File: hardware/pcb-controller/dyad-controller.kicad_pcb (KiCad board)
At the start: 2 copper layers, 35 x 50 mm, 45 parts, among them J1 USB_C_Receptacle_USB2.0, J10 USB-C split link, J2 SWD, J6 HC-FPC-0.5-20P-FH20, J7 HC-FPC-0.5-20P-FH20, J8 HC-FPC-0.5-14P-FH20, J9 USB-C split link, SW1 BOOTSEL, SW2 RESET, U1 W25Q128JVS, U2 USBLC6-2SC6, U3 RP2040, U4 XC6206PxxxMR-Regulator_Linear, Y1 12MHz

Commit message: Swap the controller crystal to the RP2040 minimal design's ABM8-272-T3
Found by the CONTROLLER.md §6 checklist, item 3. The reference design's
crystal was LCSC C9002 (YXC X322512MSB4SI): CL 20 pF and ESR 80 ohm,
loaded with 22 pF caps. That gives ~11 + 3 pF stray = ~14 pF against the
20 pF it needs, so it would run fast; and its ESR is above the 50 ohm that
Hardware design with RP2040 §2.3 assumes when sizing the 1 kOhm XOUT
resistor, so start-up margin was unknown. The guide says any other crystal
circuit "will require extensive testing".

Now the guide's circuit unchanged: Abracon ABM8-272-T3 (LCSC C20625731,
CL 10 pF, ESR <= 50 ohm) with two 15 pF C0G caps (C2/C3, LCSC C1548, JLCPCB
Basic) and R7 at 1 kOhm -- 7.5 pF + ~3 pF stray = 10.5 pF.

Same 3.2 x 2.5 mm 4-pad package with crystal on pins 1/3 and ground on
2/4, so the footprint and routing are untouched; only Y1's LCSC and
description and C2/C3's value and LCSC change, mirrored onto the board
footprints. CONTROLLER.md's BOM and §4 "transfers unchanged" list updated.

ERC unchanged at 152. DRC: 0 errors, 0 unconnected. Parity: 14.

Co-Authored-By: Claude Opus 5.5 <noreply@anthropic.com>
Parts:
- C2, C3: value 22pF -> 15pF
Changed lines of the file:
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@@
 			)
 		)
-		(property "Value" "22pF"
+		(property "Value" "15pF"
 			(at 0 -1.16 90)
 			(layer "B.Fab")
@@
 			)
 		)
-		(property "LCSC" "C1555"
+		(property "LCSC" "C1548"
 			(at 128.606875 285.547125 0)
 			(layer "B.Fab")
@@
 			)
 		)
-		(property "Value" "22pF"
+		(property "Value" "15pF"
 			(at 0 -1.16 270)
 			(layer "B.Fab")
@@
 			)
 		)
-		(property "LCSC" "C1555"
+		(property "LCSC" "C1548"
 			(at 278.590375 -122.158125 0)
 			(layer "B.Fab")
@@
 			)
 		)
-		(property "Description" ""
+		(property "Description" "Abracon ABM8-272-T3, 12 MHz, CL 10 pF, ESR 50 ohm max -- the crystal of the RP2040 minimal design"
 			(at 0 0 0)
 			(layer "F.Fab")
@@
 			)
 		)
-		(property "LCSC" "C9002"
+		(property "LCSC" "C20625731"
 			(at 0 0 0)
 			(layer "B.Fab")

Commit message: Remove the SWD header, move the RP2040 block forward, reroute with USB on B.Cu
The §6 checklist failed item 5: D+ 18 mm, D- 26 mm, six vias. Several
attempts to reroute USB in place left gaps, because the corridor from J1 to
U3 had no room for the nets that have to hop beside the pair.

- J2 (1x05 SWD socket, 13.8 x 3.6 mm through-hole) removed from schematic
  and board, with its wiring, labels and power symbols; U3's SWCLK/SWDIO
  get no-connect flags. Flashing is over USB with BOOTSEL. ERC 152 -> 145,
  no new findings.
- U3 with all its decoupling, the crystal network, R5/R6 and the flash
  with C1/R1 moved 4 mm forward as one group into the freed space; U2 a
  further 1 mm so a via fits beside its +5V pin, which sits between its
  two USB pins.
- USB routed by hand-written router on B.Cu: D+ 15.9 mm, D- 16.1 mm, no
  vias. The rest by Freerouting around it; then +5V to U2 and one GPIO1
  hop at J7 routed by the same router, 11 vias moved for hole spacing, a
  VBUS track at J1 necked to 0.3 mm, GND fills with 76 stitching vias, C13's
  GND pad solid. JLC marker moved clear of C15.

Against 2dc9af0: total track 2,167 -> 1,915 mm; F.Cu fill 48% in 5 pieces
-> 46% in 4, largest 656 -> 774 mm^2; B.Cu 47% in 16 -> 49% in 9, largest
738 -> 803 mm^2. Ground under USB 4% -> 9%, crystal 42% -> 27%, QSPI 26% ->
1% -- the matrix bundle still crosses beneath them on F.Cu.

CONTROLLER.md: J2's removal recorded, and the §6 checklist results added
(items 1-3, 8 pass; 4, 5 partial; 6, 7 open), with a correction to the
claim that no matrix crosses this board.

DRC: 0 errors, 0 unconnected. Parity: 14 field-copy differences.

Co-Authored-By: Claude Opus 5.5 <noreply@anthropic.com>
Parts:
- removed J2: SWD, Connector_PinSocket_2.54mm:PinSocket_1x05_P2.54mm_Vertical
- moved U1 4.00 mm to (207.3, 65.4)
- moved C1 4.00 mm to (204.2, 61.6)
- moved C10 4.00 mm to (200.5, 81.6)
- moved C11 4.00 mm to (194.1, 77.0)
- moved C12 4.00 mm to (207.6, 76.2)
- moved C14 4.00 mm to (194.9, 69.1)
- moved C15 4.00 mm to (206.6, 70.4)
- moved C2 4.00 mm to (207.1, 85.5)
- moved C3 4.00 mm to (200.4, 85.2)
- moved C5 4.00 mm to (199.9, 66.0)
- moved C6 4.00 mm to (198.9, 81.6)
- moved C9 4.00 mm to (194.9, 70.6)
- moved R1 4.00 mm to (210.9, 61.4)
- moved R5 4.00 mm to (201.1, 63.0)
- moved R6 4.00 mm to (199.3, 63.0)
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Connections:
- U3 pad 24: SWCLK -> unconnected-(U3-SWCLK-Pad24)
- U3 pad 25: SWD -> unconnected-(U3-SWDIO-Pad25)
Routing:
- net /GPIO12: track 86.8 -> 39.8 mm, vias 5 -> 3
- net SWCLK: track 26.6 -> 0.00 mm, vias 2 -> 0
- net /GPIO8: track 81.2 -> 55.8 mm
- net SWD: track 25.1 -> 0.00 mm
- net /GPIO15: track 74.6 -> 51.1 mm, vias 5 -> 2
- net GND: track 330.2 -> 307.1 mm, vias 76 -> 78
- net /GPIO4: track 54.4 -> 74.9 mm, vias 3 -> 4
- net /GPIO3: track 71.3 -> 51.6 mm, vias 5 -> 4
- net /GPIO14: track 72.1 -> 53.8 mm, vias 6 -> 4
- net /GPIO9: track 55.6 -> 39.0 mm, vias 4 -> 3
- net /GPIO13: track 66.2 -> 52.3 mm, vias 2 -> 5
- net /VBUS_SPLIT: track 57.0 -> 45.1 mm, vias 2 -> 3
- net /GPIO0: track 51.3 -> 62.5 mm
- net D_USB_N: track 15.2 -> 4.72 mm, vias 2 -> 0
- net /GPIO1: track 39.5 -> 49.8 mm
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
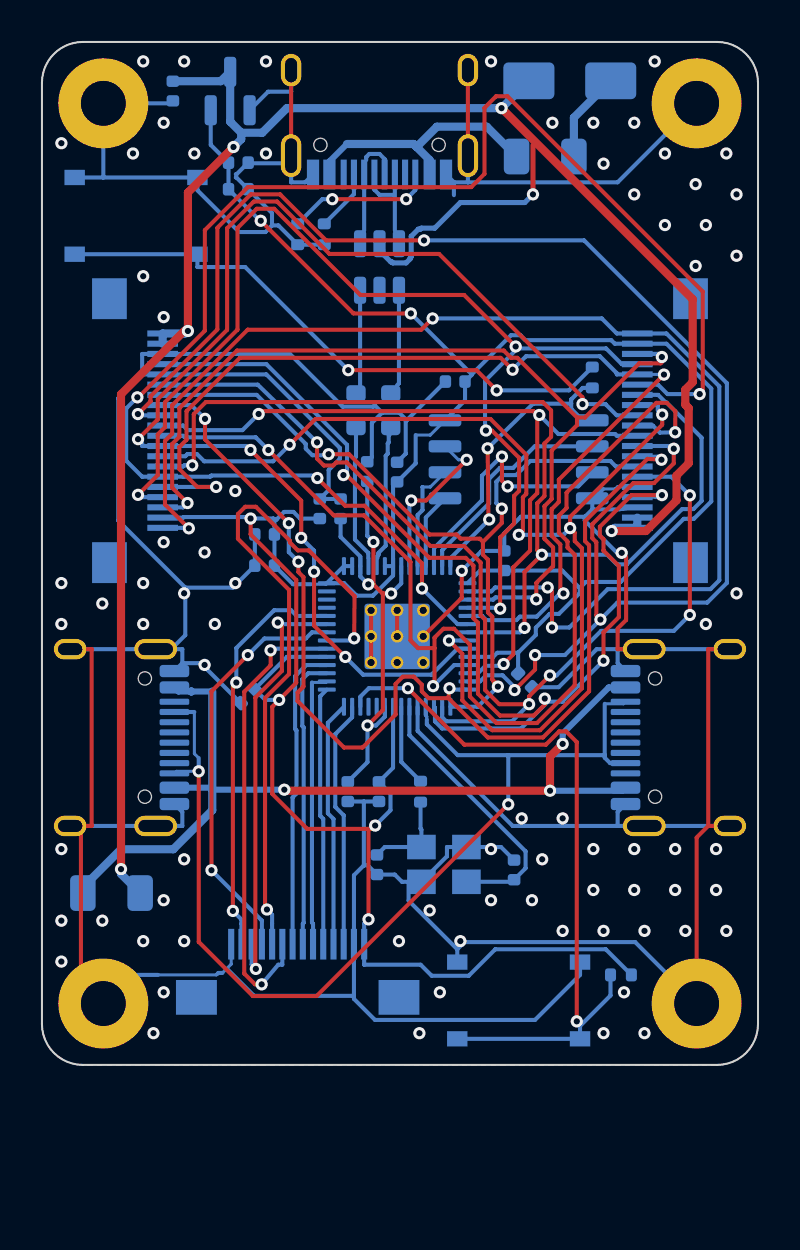
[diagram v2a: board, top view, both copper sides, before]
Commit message: Hand-reroute matrix lines to clear F.Cu under the RP2040
Rerouted by hand in KiCad: GPIO2, GPIO4, GPIO7, GPIO10 and GPIO15 shortened
by 8-18 mm each, pulling F.Cu copper out from under the RP2040's
surroundings. USB is untouched (D+ 15.9 mm / D- 16.1 mm, B.Cu, no vias).

Against 87c2ec7: F.Cu GND fill 46% -> 58% of the board, main piece 774 ->
987 mm^2; B.Cu 49% -> 51%, main piece 803 -> 833 mm^2. Ground under the fast
nets on the opposite layer: USB 9% -> 28%, crystal 27% -> 50%, QSPI 1%
(unchanged -- its lines still run over the remaining bundle crossing).

Also removes a 0.017 mm dangling GPIO15 stub left by the interactive router.
CONTROLLER.md §6 results updated to these figures.

DRC: 0 errors, 0 unconnected (unchanged by a refill, so the saved fill was
current). Parity: 14 field-copy differences. ERC: 145.

Co-Authored-By: Claude Opus 5.5 <noreply@anthropic.com>
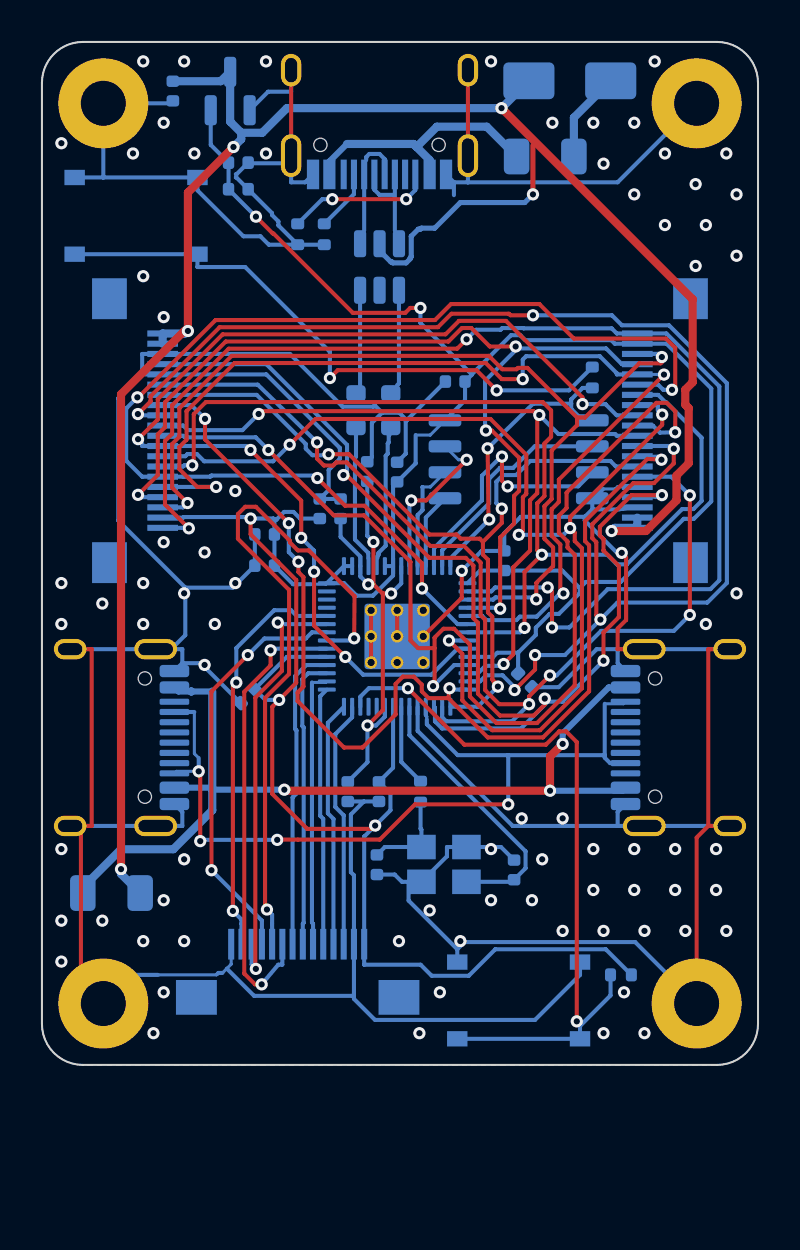
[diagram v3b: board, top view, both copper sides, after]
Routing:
- net /GPIO4: track 74.9 -> 57.1 mm
- net /GPIO15: track 51.1 -> 41.9 mm, vias 2 -> 4
- net /GPIO10: track 79.5 -> 71.7 mm
- net /GPIO7: track 61.9 -> 54.2 mm
- net /GPIO2: track 55.6 -> 47.9 mm
- net /~{USB_BOOT}: track 28.9 -> 30.0 mm
- net +3V3: track 146.4 -> 147.4 mm, vias 6 -> 5
- net /GPIO3: track 51.6 -> 52.3 mm

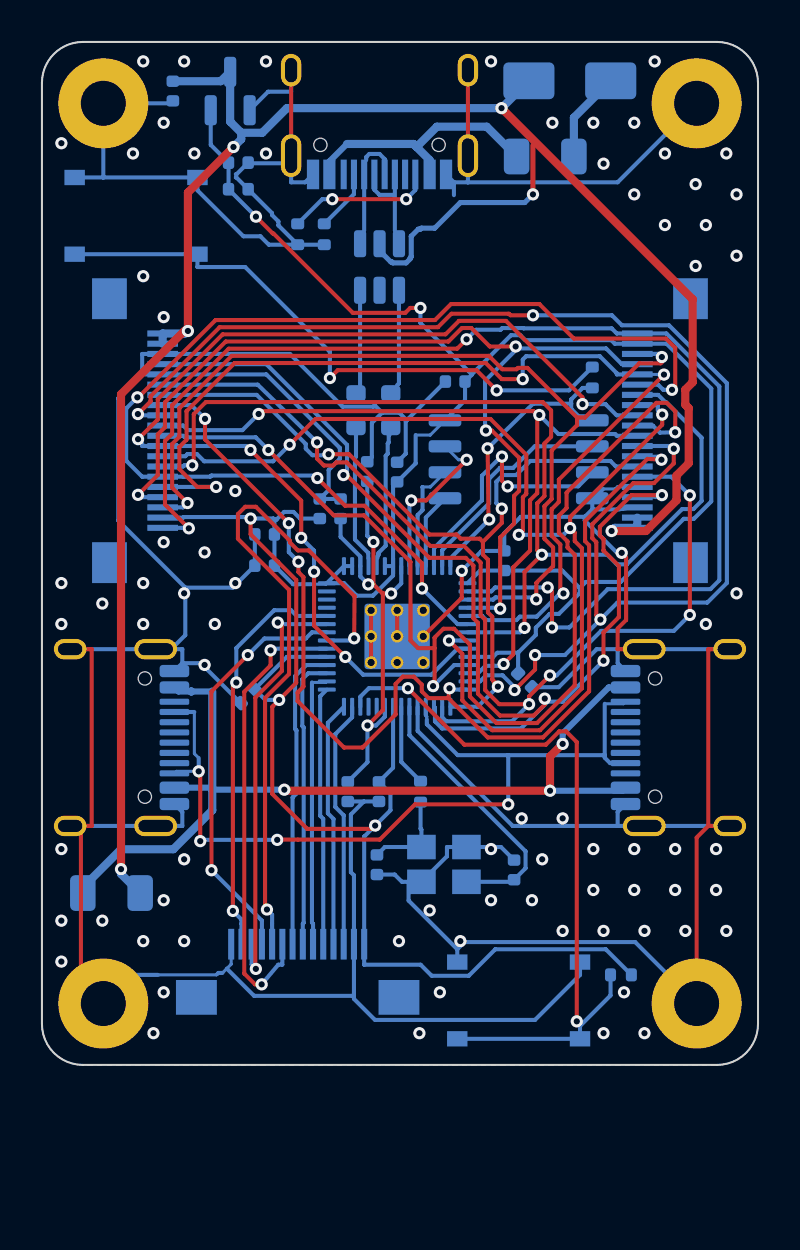
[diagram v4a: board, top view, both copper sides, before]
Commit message: WIP: 35 x 57 controller, rerouted -- GPIO3 left to hand-route
Work in progress, to be finished by hand in KiCad. Not for merging as-is.

Board lengthened from 50 to 57 mm (outline y 45-102). J6/J7 moved 7 mm
down to the RP2040's height, J9/J10 7 mm down below them, the front zone
(J8, F2, H3/H4) 7 mm down; SW2 + R2 moved up to the right edge below H2;
SW1 moved down the left edge to clear the rear-left corner around J1.

Routing: USB by the grid router on B.Cu (D+ 15.9 / D- 16.1 mm, no vias,
locked), the rest by Freerouting with a via-to-via clearance of 0.25 mm
added to the DSN -- which keeps holes >= 0.55 mm apart, so no hole-to-hole
fixes were needed at all. GND fills on both layers, 120 stitching vias;
J9's shell and C5's GND pad connect solid.

Left for KiCad: GPIO3 (COL5) is unrouted -- U3 pin 5 to J7 pad 5, and
across to its 1 mm stub at J6 pad 5 (a dangling GPIO3 via sits there).
Three Freerouting runs and the grid router found no path: pin 5 is boxed in
by GPIO2/GPIO5's fan-out, and no corridor across the board is free, so a
neighbouring line or two will need to move.

Measured with GPIO3 open, against the 35 x 50 board (b6add58): ground under
USB 28 -> 35%, crystal 50 -> 77%, QSPI 1 -> 0%; F.Cu fill 58 -> 55% (main
piece 987 -> 1061 mm^2), B.Cu 51 -> 52% in 7 pieces instead of 9.

Not yet updated for 57 mm: interface.yaml (envelope, front hole positions
y 47 -> 54), the outline DXF and generator script, CONTROLLER.md.

DRC: 0 errors; unconnected = GPIO3's 2 only. Parity: 14.

Co-Authored-By: Claude Opus 5.5 <noreply@anthropic.com>
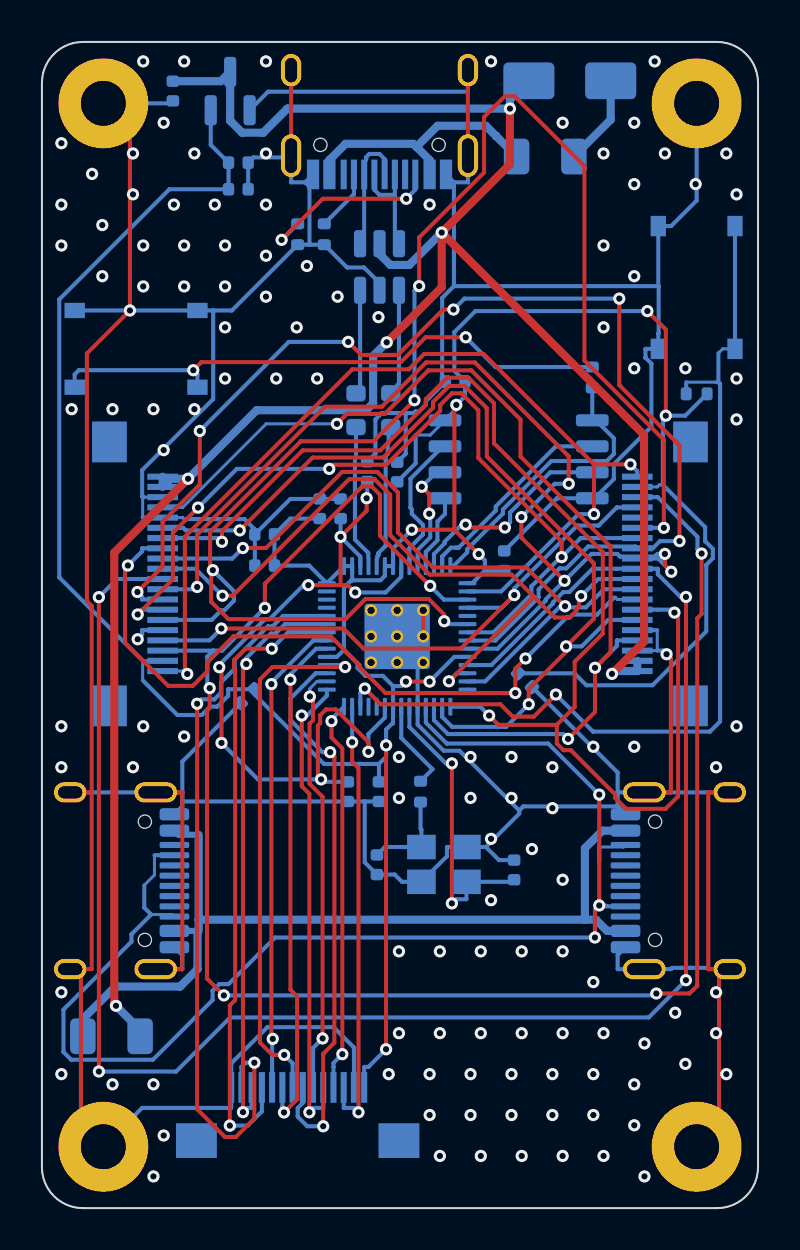
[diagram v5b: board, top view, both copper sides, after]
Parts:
- moved SW2 35.9 mm to (216.0, 57.0), turned to 90 degrees
- moved R2 28.6 mm to (216.0, 62.2)
- moved F2 7.00 mm to (187.4, 93.6)
- moved H3 7.00 mm to (187.0, 99.0)
- moved H4 7.00 mm to (216.0, 99.0)
- moved J10 7.00 mm to (186.4, 86.0)
- moved J6 7.00 mm to (188.6, 71.0)
- moved J7 7.00 mm to (214.4, 71.0)
- moved J8 7.00 mm to (196.5, 97.4)
- moved J9 7.00 mm to (216.6, 86.0)
- moved SW1 6.50 mm to (188.6, 60.0)
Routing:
- net /GPIO3: track 52.3 -> 1.54 mm, vias 4 -> 1
- net /GPIO1: track 49.6 -> 89.0 mm, vias 3 -> 6
- net /GPIO10: track 71.7 -> 35.5 mm, vias 6 -> 2
- net /GPIO8: track 55.8 -> 89.3 mm, vias 3 -> 4
- net GND: track 307.6 -> 336.2 mm, vias 78 -> 122
- net /GPIO12: track 39.8 -> 64.5 mm
- net /GPIO15: track 41.9 -> 66.1 mm, vias 4 -> 3
- net /GPIO4: track 57.1 -> 78.5 mm, vias 4 -> 5
- net /GPIO2: track 47.9 -> 29.4 mm, vias 4 -> 2
- net +1V1: track 23.2 -> 40.0 mm, vias 4 -> 8
- net /GPIO26: track 20.0 -> 36.7 mm
- net /GPIO0: track 62.1 -> 46.7 mm, vias 4 -> 3
- net +3V3: track 147.4 -> 162.5 mm, vias 5 -> 9
- net /GPIO11: track 54.2 -> 39.4 mm, vias 5 -> 3
- net /GPIO20: track 14.3 -> 27.5 mm, vias 0 -> 2
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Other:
- board size 35 x 50 mm -> 35 x 57 mm

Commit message: Swap the side connectors on the 35 x 57 controller and reroute it complete
Replaces the WIP routing of bf3d8a0, which left GPIO3 unroutable.

Placement: on each side edge the split USB-C now sits above the main FFC --
J10/J9 at y 29 from the rear edge, J6/J7 at y 41.8 -- so the 20-pin FFCs
get the roomier lower half. F2 moves above J10, next to the port it feeds.

Routing, with hardware/route_tools.py: USB by the grid router on B.Cu
(D+ 15.9 / D- 16.1 mm, no vias), the rest by Freerouting with the 0.25 mm
via-to-via DSN rule -- complete, GPIO3 included; one via nudged 0.02 mm off
J9's peg hole. GND fills on both layers, 135 stitching vias.

Against the 35 x 50 board of PR #1, ground under the fast nets (GND fill on
the opposite layer along each track): USB 28% -> 82%, QSPI 1% -> 65%,
crystal 50% -> 46%. F.Cu fill 58% -> 65% of the board, main piece 987 ->
1,149 mm^2. With the FFCs low, the matrix bundle no longer crosses under the
USB and QSPI routing on F.Cu.

Follow-ups for the 57 mm board:
- interface.yaml v13: envelope [57, 35], front holes y 47 -> 54, connector
  positions on the board recorded in the changelog.
- Outline DXF regenerated (35 x 57) and generate_controller_outline.py.
- CONTROLLER.md: as-built side-edge order, edge budget, §6 checklist (item
  5 now largely met) with the three-routing comparison.
- TOOLS.md: the via-to-via rule, the junction-via trap, the scratchpad loss.

DRC: 0 errors, 0 unconnected; silkscreen fully on the board. Parity: 14.
Fab outputs re-exported (gitignored): Gerbers, left/right BOM and CPL.

Co-Authored-By: Claude Opus 5.5 <noreply@anthropic.com>
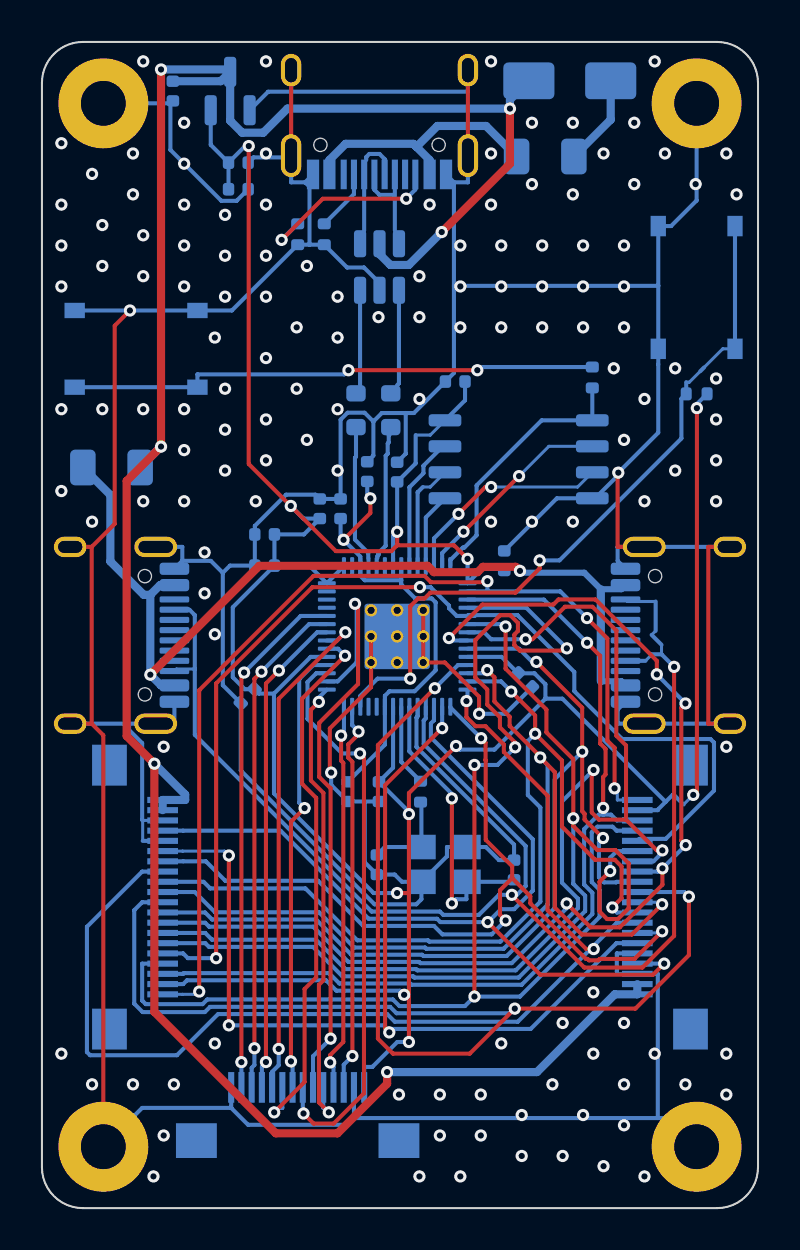
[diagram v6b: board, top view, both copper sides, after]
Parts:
- moved F2 27.8 mm to (187.4, 65.8)
- moved J6 15.8 mm to (188.6, 86.8)
- moved J7 15.8 mm to (214.4, 86.8)
- moved J10 12.0 mm to (186.4, 74.0)
- moved J9 12.0 mm to (216.6, 74.0)
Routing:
- net /GPIO3: track 1.54 -> 53.3 mm, vias 1 -> 2
- net /GPIO1: track 89.0 -> 45.6 mm, vias 6 -> 2
- net /GPIO2: track 29.4 -> 66.0 mm, vias 2 -> 4
- net /GPIO4: track 78.5 -> 52.3 mm, vias 5 -> 3
- net /GPIO12: track 64.5 -> 41.6 mm
- net /GPIO8: track 89.3 -> 68.5 mm, vias 4 -> 3
- net /GPIO11: track 39.4 -> 56.8 mm, vias 3 -> 2
- net +1V1: track 40.0 -> 23.0 mm, vias 8 -> 2
- net /GPIO5: track 43.6 -> 55.9 mm, vias 4 -> 3
- net /GPIO9: track 38.1 -> 49.9 mm
- net ~{RESET}: track 47.4 -> 35.6 mm
- net /GPIO26: track 36.7 -> 25.5 mm
- net /GPIO10: track 35.5 -> 46.3 mm, vias 2 -> 3
- net /GPIO19: track 21.1 -> 29.8 mm
- net /GPIO24: track 31.0 -> 23.8 mm
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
